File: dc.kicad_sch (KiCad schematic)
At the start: 8 parts, among them J9 J_PWR_11-25V, U1 LDO_3V3_ISO, U2 NCM3S1205MC, U3 NCM3S1205MC

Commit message: Regles de clearance par domaine d'isolement et filtre EMC recommande sur les NCM3S1205MC
Ajoute deux netclasses (Isole_Primaire/Isole_Secondaire, assignees par nom
de net) et une regle shield.kicad_dru qui impose 8mm de clearance des
qu'une paire traverse les deux domaines - valeur issue du datasheet
Murata (UL62368-1, 2 MOPP, 250Vrms), pas estimee. Rien n'existait avant
pour differencier electriquement primaire et secondaire au DRC.

Ajoute le filtre EMC recommande par le datasheet (p.8) sur l'entree des
deux NCM3S1205MC (L1-L4, C26-C35), ce qui a necessite de renommer les
labels VIN_PWR/GND_PRI au niveau des pins VIN de U2/U3 vers des noeuds
intermediaires dedies (U2_VINF/U2_GNDF, U3_VINF/U3_GNDF).

Co-Authored-By: Claude Sonnet 5 <noreply@anthropic.com>
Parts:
- added C24, C25: 100nF, Capacitor_SMD:C_0805_2012Metric, symbol Device:C
- added C26, C27, C31, C32: 22uF, Capacitor_SMD:C_0805_2012Metric, symbol Device:C
- added C28, C33: 220pF, Capacitor_SMD:C_0805_2012Metric, symbol Device:C
- added C29, C30, C34, C35: 470pF, Capacitor_SMD:C_0805_2012Metric, symbol Device:C
- added L1, L2, L3, L4: 22uH, Inductor_SMD:L_0805_2012Metric, symbol Device:L
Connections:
- net 3V3_ISO: now also C25.1
- net 5V_ISO: now also C29.1, C30.1
- net 5V_ISO_SW: now also C24.1
- net 5V_NUM: now also C34.1, C35.1
- net GND: now also C24.2, C25.2, C29.2, C30.2, C34.2, C35.2
- net GND_PRI: now also L2.1, L4.1; no longer U2.2 (+Vin), U3.2 (+Vin)
- net VIN_PWR: now also L1.1, L3.1; no longer U2.1 (-Vin), U3.1 (-Vin)
- new net U2_GNDF: C26.2, C27.2, C28.2, L2.2, U2.2 (+Vin)
- new net U2_VINF: C26.1, C27.1, C28.1, L1.2, U2.1 (-Vin)
- new net U3_GNDF: C31.2, C32.2, C33.2, L4.2, U3.2 (+Vin)
- new net U3_VINF: C31.1, C32.1, C33.1, L3.2, U3.1 (-Vin)

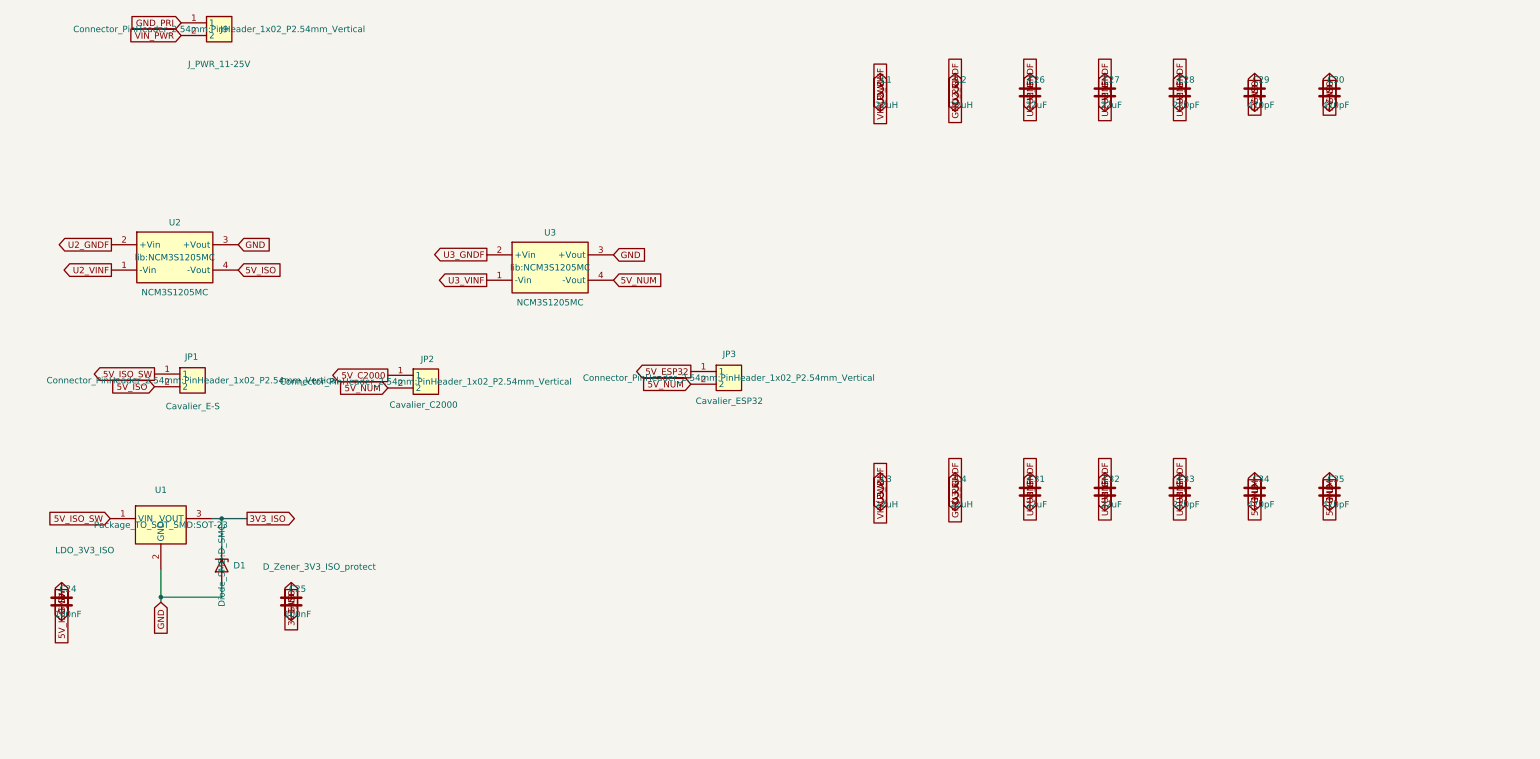
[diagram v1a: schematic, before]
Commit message: Gabarit de netclasses, filtre EMC NCM3S1205MC, embase OLED, et groupement/routage des 23 trios de protection
- shield.kicad_pro : 8 netclasses (Default/Rapide/Analogique/Alim/Isole_Primaire/
  Isole_Secondaire/Puissance/HT), 83 motifs de net classes
- dc.kicad_sch : filtre EMC d'entree (L1-L4, C26-C28, C31-C33) pour les deux
  NCM3S1205MC ; etage de sortie (C4/C5 du datasheet) volontairement omis
  (decision #16, doc/decisions.md)
- connecteur_devkit.kicad_sch : embase OLED J10 (IDC 2x8 detrompee),
  symbole mecanique U4 (ER-OLEDM032-1), correction label 3V3_ESP32
- shield.kicad_pcb : les 23 trios de protection (BAT54S+R+C) groupes,
  routes (GND + signal interne), retournes en B.Cu pour matcher le
  gabarit, places en couronne hors carte pour placement/routage manuel
- doc/nappes-shield.md, doc/decisions.md : mis a jour en consequence

Co-Authored-By: Claude Sonnet 5 <noreply@anthropic.com>
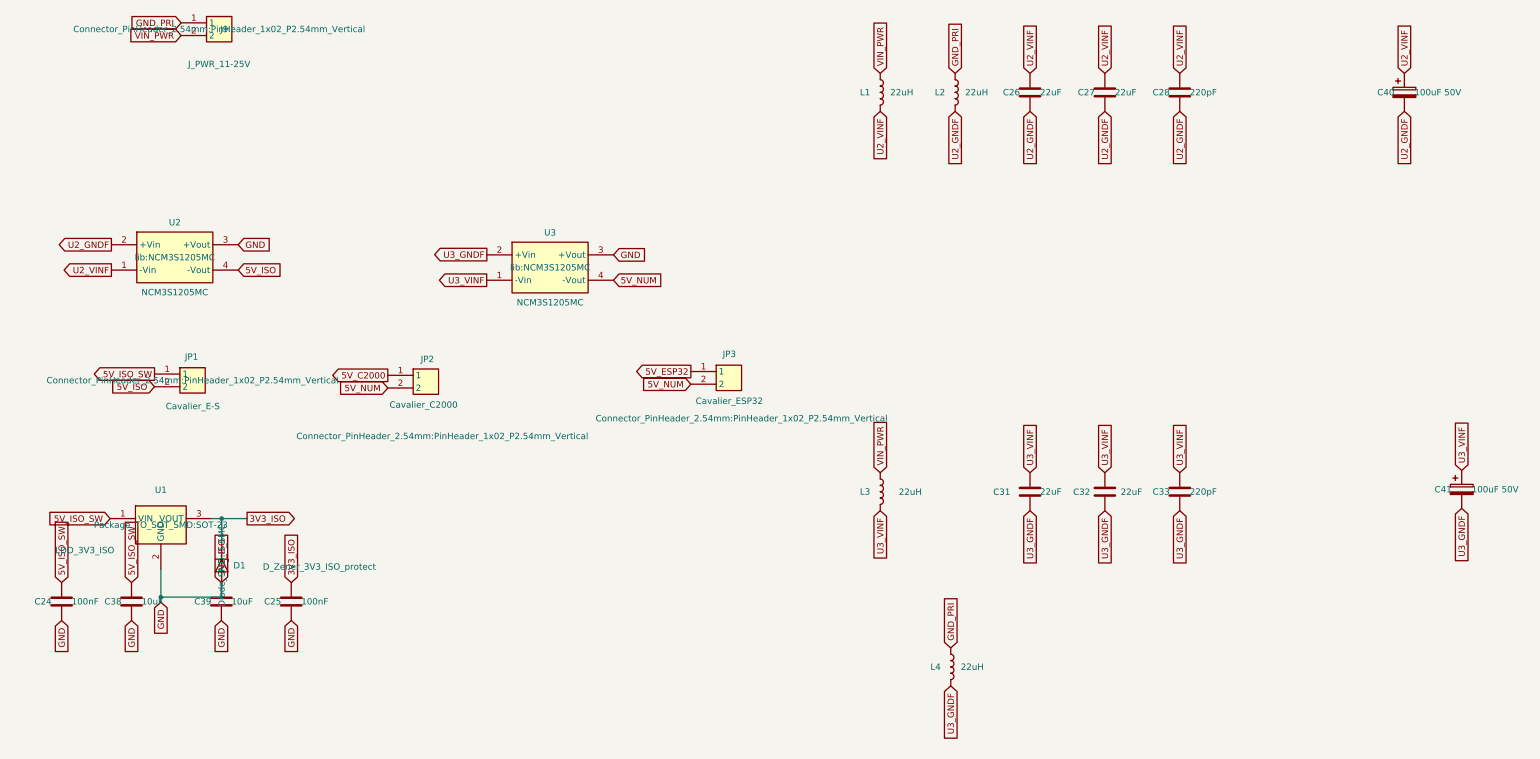
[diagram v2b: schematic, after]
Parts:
- removed C29, C30, C34, C35: 470pF, Capacitor_SMD:C_0805_2012Metric, symbol Device:C
- added C38, C39: 10uF, Capacitor_SMD:C_0805_2012Metric, symbol Device:C
- added C40, C41: 100uF 50V, Capacitor_SMD:CP_Elec_8x10.5, symbol Device:C_Polarized
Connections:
- net 3V3_ISO: now also C39.1
- net 5V_ISO_SW: now also C38.1
- net GND: now also C38.2, C39.2
- net U2_GNDF: now also C40.2
- net U2_VINF: now also C40.1
- net U3_GNDF: now also C41.2
- net U3_VINF: now also C41.1
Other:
- moved on the sheet: L4
